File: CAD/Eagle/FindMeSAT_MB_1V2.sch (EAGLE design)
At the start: 135 parts, among them Q101 ABS07-32.768KHZ, Q651 ABM3B-16MHZ-10-R50-1-U, U1001 CFPT-141-20MHZ, U101 ATXMEGA256A3BU-AU, U1011 OPA354, U1021 OPA354, U1111 LM2831YMF, U1121 LM4120IM5-3.0, U201 SIM808, U301 MPU-9250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

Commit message: HW_V1.2 - GSM antenna dimension (ADS), miter at busses, wire width in respect to 0.120 mm prepreg height - BT antenna still to do
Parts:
- R271, R281: device rcl:R-EU_R0603 -> rcl:R-EU_R0805
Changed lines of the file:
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@@
 <class number="1" name="pwr2A" width="0.8" drill="0">
 </class>
-<class number="2" name="R50" width="0.4064" drill="0">
+<class number="2" name="R50" width="0.2032" drill="0">
 <clearance class="2" value="0.9"/>
 </class>
-<class number="3" name="R90_USB" width="0.2921" drill="0">
+<class number="3" name="R90_USB" width="0.15" drill="0">
 <clearance class="3" value="0.2032"/>
 </class>
 <class number="4" name="pwrA5" width="0.4" drill="0">
 </class>
-<class number="5" name="R75" width="0.1524" drill="0">
+<class number="5" name="R75" width="0.15" drill="0">
 <clearance class="5" value="0.2032"/>
 </class>
@@
 <part name="R171" library="rcl" deviceset="R-EU_" device="R0603" value="68R"/>
 <part name="R222" library="rcl" deviceset="R-EU_" device="R0603" value="68R"/>
-<part name="R271" library="rcl" deviceset="R-EU_" device="R0603"/>
-<part name="R281" library="rcl" deviceset="R-EU_" device="R0603"/>
+<part name="R271" library="rcl" deviceset="R-EU_" device="R0805"/>
+<part name="R281" library="rcl" deviceset="R-EU_" device="R0805"/>
 <part name="R291" library="rcl" deviceset="R-EU_" device="R0603"/>
 <part name="C291" library="rcl" deviceset="C-EU" device="C0603"/>

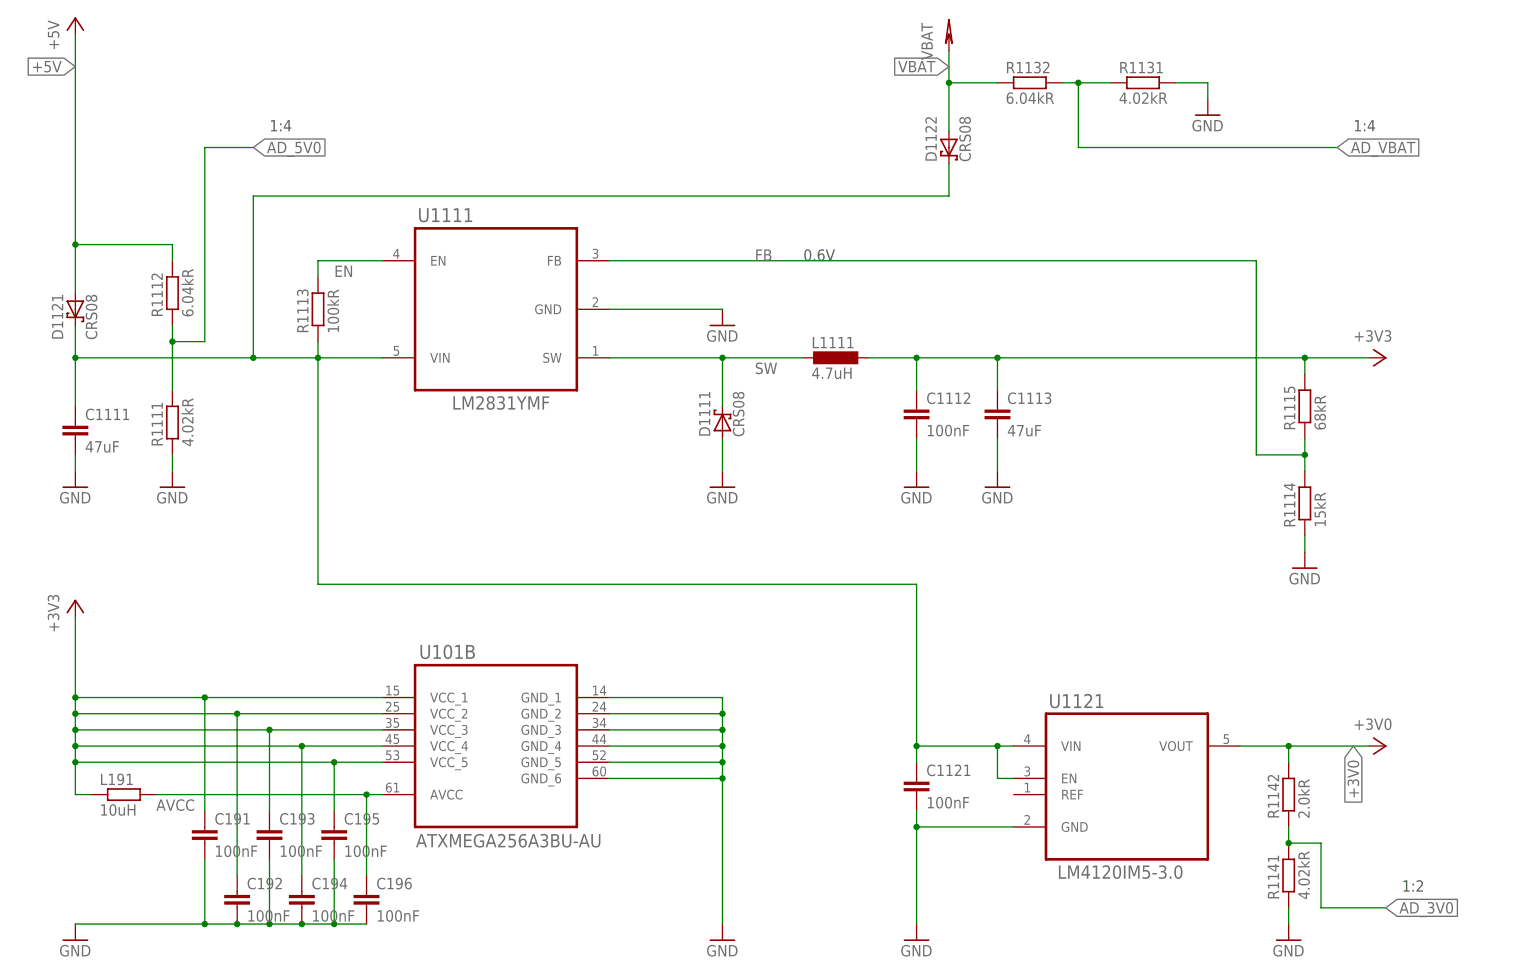
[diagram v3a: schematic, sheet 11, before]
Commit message: HW_V1.2 - PWM low pass filter needs 10uF instead of 100nF, ADC measuring levels are 2.0V
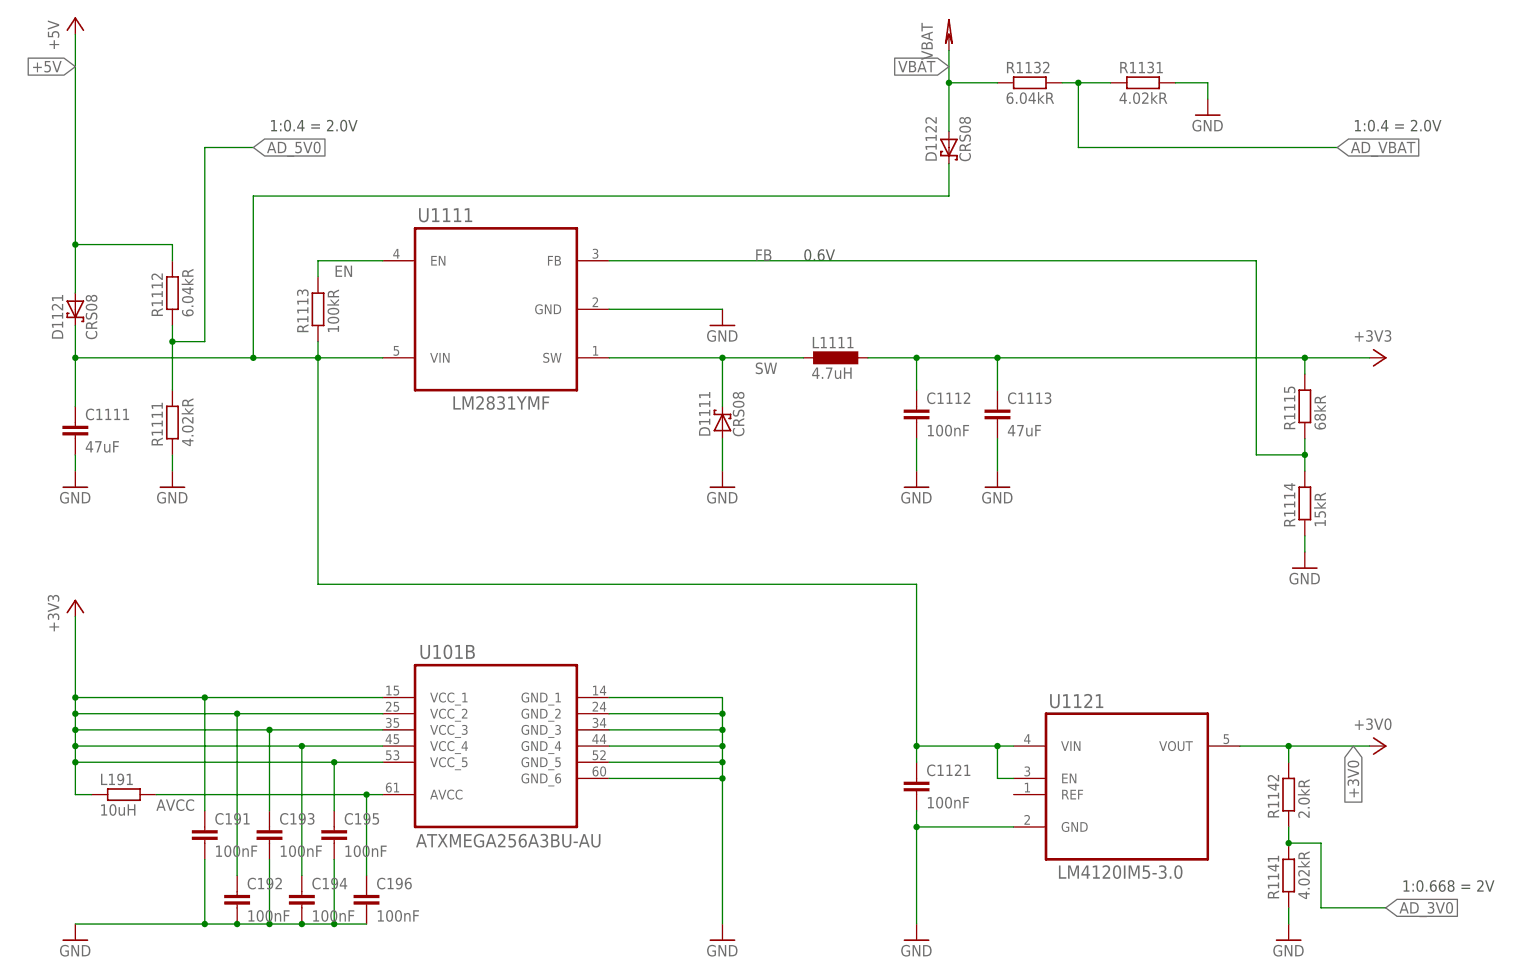
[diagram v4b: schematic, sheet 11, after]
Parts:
- C1001: value 100nF -> 10uF
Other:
- note added: "1:0.4 = 2.0V"
- note added: "1:0.668 = 2V"
- note added: "f_LP = 1 Hz, PWM min. 100 Hz"
- note removed: "1:2"
- note removed: "1:4"
- note removed: "f_LP = 15 Hz"
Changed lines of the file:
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@@
 <part name="C1002" library="rcl" deviceset="C-EU" device="C0603" value="100nF"/>
 <part name="+3V0_1001" library="df4iah_supply" deviceset="+3V0" device=""/>
-<part name="C1001" library="rcl" deviceset="C-EU" device="C0603" value="100nF"/>
+<part name="C1001" library="rcl" deviceset="C-EU" device="C0603" value="10uF"/>
 <part name="R1001" library="rcl" deviceset="R-EU_" device="R0603" value="100kR"/>
 <part name="GND1001" library="df4iah_supply" deviceset="GND" device=""/>
@@
 <description>VCTCXO</description>
 <plain>
-<text x="35.56" y="127" size="1.778" layer="97">f_LP = 15 Hz</text>
+<text x="35.56" y="127" size="1.778" layer="97">f_LP = 1 Hz, PWM min. 100 Hz</text>
 <text x="144.78" y="116.84" size="1.778" layer="97">580mV</text>
 </plain>
@@
 <plain>
 <text x="139.7" y="134.62" size="1.778" layer="97">0.6V</text>
-<text x="55.88" y="154.94" size="1.778" layer="97">1:4</text>
-<text x="233.68" y="35.56" size="1.778" layer="97">1:2</text>
-<text x="226.06" y="154.94" size="1.778" layer="97">1:4</text>
+<text x="55.88" y="154.94" size="1.778" layer="97">1:0.4 = 2.0V</text>
+<text x="233.68" y="35.56" size="1.778" layer="97">1:0.668 = 2V</text>
+<text x="226.06" y="154.94" size="1.778" layer="97">1:0.4 = 2.0V</text>
 </plain>
 <instances>

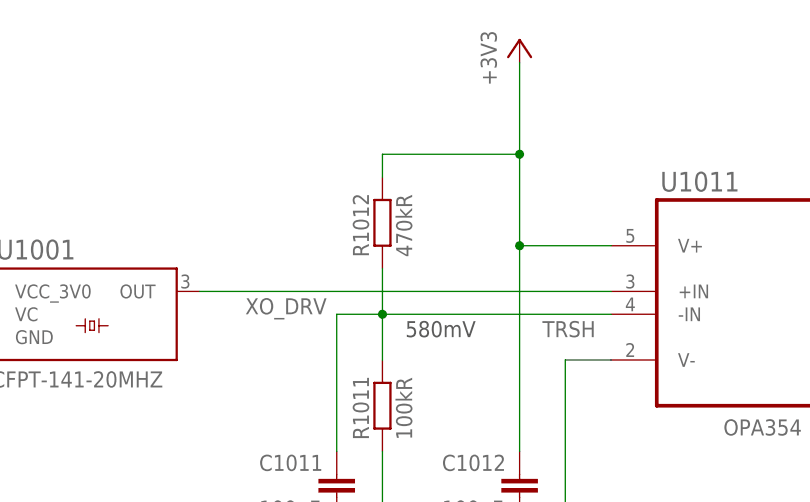
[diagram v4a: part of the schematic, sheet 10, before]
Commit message: HW_V1.2 - OPA354 needs higher comparator voltage for 50% duty cycle
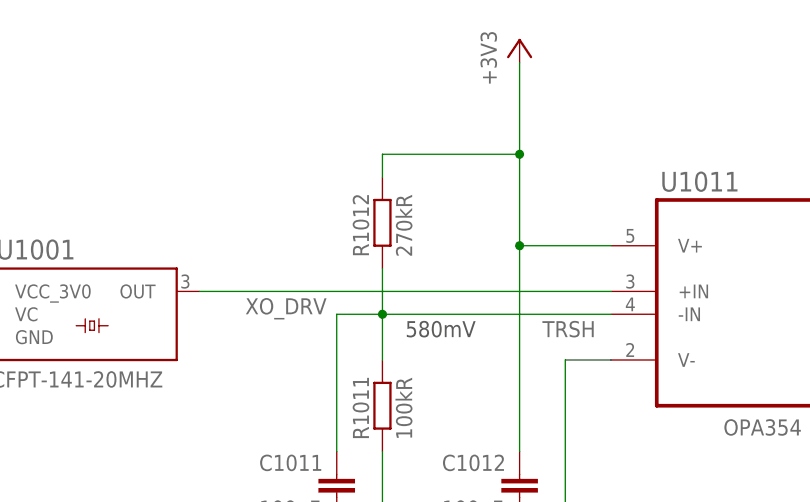
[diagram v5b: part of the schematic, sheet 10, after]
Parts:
- R1012: value 470kR -> 270kR
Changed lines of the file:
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@@
 <part name="C1012" library="rcl" deviceset="C-EU" device="C0603" value="100nF"/>
 <part name="+3V3_1011" library="df4iah_supply" deviceset="+3V3" device=""/>
-<part name="R1012" library="rcl" deviceset="R-EU_" device="R0603" value="470kR"/>
+<part name="R1012" library="rcl" deviceset="R-EU_" device="R0603" value="270kR"/>
 <part name="R1011" library="rcl" deviceset="R-EU_" device="R0603" value="100kR"/>
 <part name="GND1011" library="df4iah_supply" deviceset="GND" device=""/>

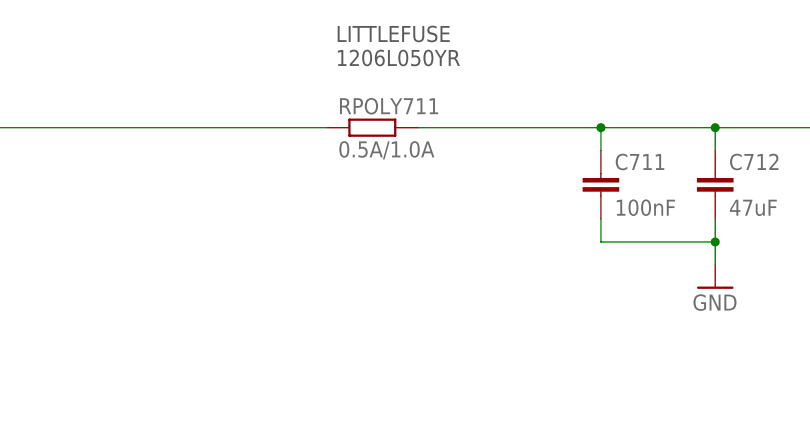
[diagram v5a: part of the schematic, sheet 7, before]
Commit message: HW_V1.2 - Polyfuse of USB - value changed from 0.5A/1.0A to 1.1A/2.2A
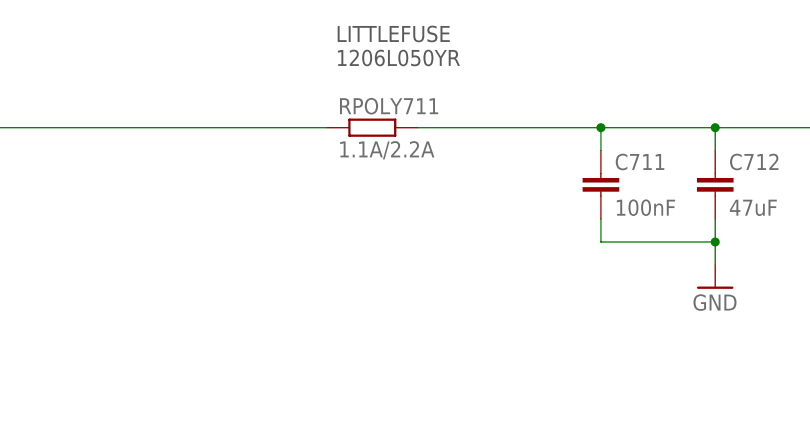
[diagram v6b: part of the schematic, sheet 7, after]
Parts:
- RPOLY711: value 0.5A/1.0A -> 1.1A/2.2A
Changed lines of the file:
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@@
 <part name="GND1203" library="df4iah_supply" deviceset="GND" device=""/>
 <part name="GND701" library="df4iah_supply" deviceset="GND" device=""/>
-<part name="RPOLY711" library="rcl" deviceset="R-EU_" device="M1206" value="0.5A/1.0A"/>
+<part name="RPOLY711" library="rcl" deviceset="R-EU_" device="M1206" value="1.1A/2.2A"/>
 <part name="R722" library="rcl" deviceset="R-EU_" device="R0603" value="68R"/>
 <part name="R723" library="rcl" deviceset="R-EU_" device="R0603" value="68R"/>

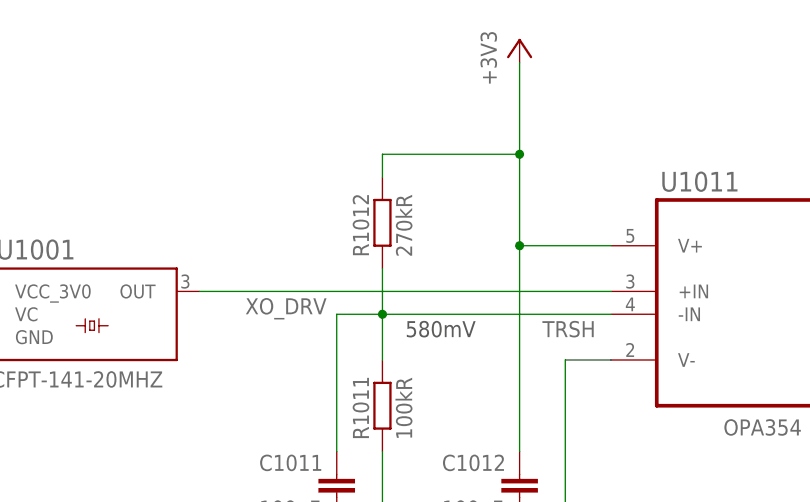
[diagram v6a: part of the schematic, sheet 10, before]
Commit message: HW_V1.2 - multiple missing fixes added (Hygro-Reset, R1141: 4.02kR --> 100pF, other value changes
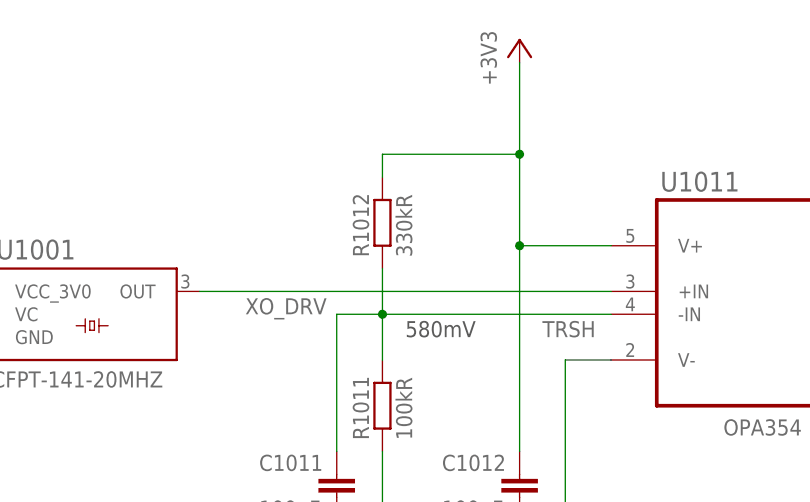
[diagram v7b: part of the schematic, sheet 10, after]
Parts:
- R1012: value 270kR -> 330kR
- R1141: value 4.02kR -> 100pF
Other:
- note added: "<-- cut nRESET line here!"
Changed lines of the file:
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@@
 <part name="C1012" library="rcl" deviceset="C-EU" device="C0603" value="100nF"/>
 <part name="+3V3_1011" library="df4iah_supply" deviceset="+3V3" device=""/>
-<part name="R1012" library="rcl" deviceset="R-EU_" device="R0603" value="270kR"/>
+<part name="R1012" library="rcl" deviceset="R-EU_" device="R0603" value="330kR"/>
 <part name="R1011" library="rcl" deviceset="R-EU_" device="R0603" value="100kR"/>
 <part name="GND1011" library="df4iah_supply" deviceset="GND" device=""/>
@@
 <part name="R1111" library="rcl" deviceset="R-EU_" device="R0603" value="4.02kR"/>
 <part name="GND1112" library="df4iah_supply" deviceset="GND" device=""/>
-<part name="R1141" library="rcl" deviceset="R-EU_" device="R0603" value="4.02kR"/>
+<part name="R1141" library="rcl" deviceset="R-EU_" device="R0603" value="100pF"/>
 <part name="GND1141" library="df4iah_supply" deviceset="GND" device=""/>
 <part name="U1021" library="df4iah_opamp" deviceset="OPA354" device=""/>
@@
 <plain>
 <text x="104.14" y="68.58" size="1.778" layer="97">I2C address = 1000100</text>
+<text x="143.764" y="90.424" size="1.778" layer="97">&lt;-- cut nRESET line here!</text>
 </plain>
 <instances>

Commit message: HW_V1.2 - missing values for antenna matching circuits added
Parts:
- C271, C272, C281, C282, C291, C292: value (none) -> 0pF
- R271, R281, R291: value (none) -> 0R
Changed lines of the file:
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@@
 <part name="R171" library="rcl" deviceset="R-EU_" device="R0603" value="68R"/>
 <part name="R222" library="rcl" deviceset="R-EU_" device="R0603" value="68R"/>
-<part name="R271" library="rcl" deviceset="R-EU_" device="R0805"/>
-<part name="R281" library="rcl" deviceset="R-EU_" device="R0805"/>
-<part name="R291" library="rcl" deviceset="R-EU_" device="R0603"/>
-<part name="C291" library="rcl" deviceset="C-EU" device="C0603"/>
-<part name="C292" library="rcl" deviceset="C-EU" device="C0603"/>
-<part name="C271" library="rcl" deviceset="C-EU" device="C0603"/>
-<part name="C281" library="rcl" deviceset="C-EU" device="C0603"/>
-<part name="C272" library="rcl" deviceset="C-EU" device="C0603"/>
-<part name="C282" library="rcl" deviceset="C-EU" device="C0603"/>
+<part name="R271" library="rcl" deviceset="R-EU_" device="R0805" value="0R"/>
+<part name="R281" library="rcl" deviceset="R-EU_" device="R0805" value="0R"/>
+<part name="R291" library="rcl" deviceset="R-EU_" device="R0603" value="0R"/>
+<part name="C291" library="rcl" deviceset="C-EU" device="C0603" value="0pF"/>
+<part name="C292" library="rcl" deviceset="C-EU" device="C0603" value="0pF"/>
+<part name="C271" library="rcl" deviceset="C-EU" device="C0603" value="0pF"/>
+<part name="C281" library="rcl" deviceset="C-EU" device="C0603" value="0pF"/>
+<part name="C272" library="rcl" deviceset="C-EU" device="C0603" value="0pF"/>
+<part name="C282" library="rcl" deviceset="C-EU" device="C0603" value="0pF"/>
 <part name="GND292" library="df4iah_supply" deviceset="GND" device=""/>
 <part name="GND293" library="df4iah_supply" deviceset="GND" device=""/>
